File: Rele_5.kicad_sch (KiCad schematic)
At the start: 6 parts, among them J15 Rele_5, J32 Pin GND, K4 SRD-05VDC-SL-C, Q12 PMBT3904,235

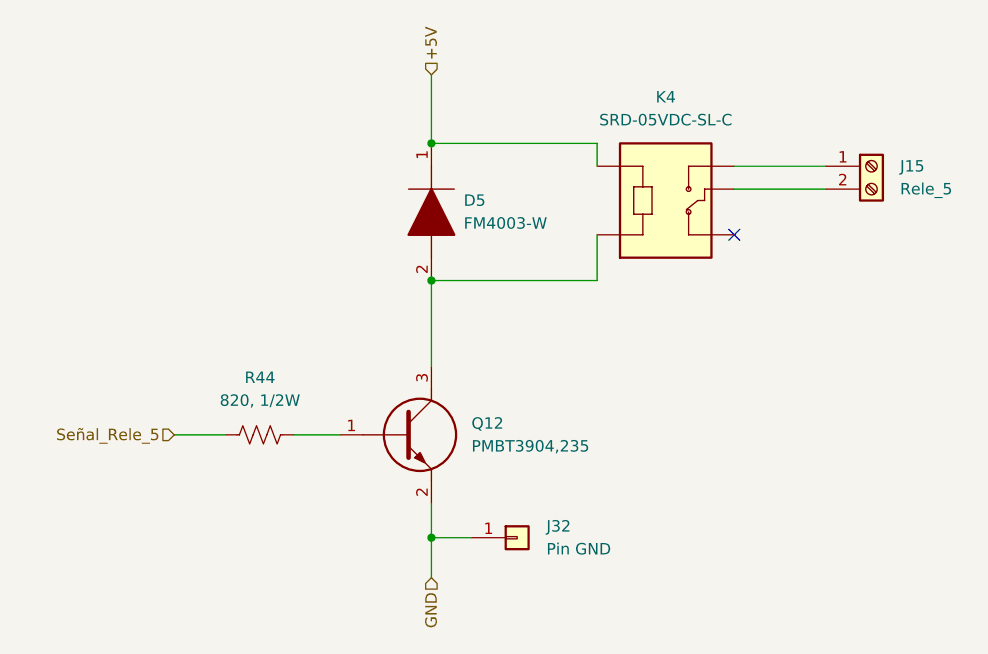
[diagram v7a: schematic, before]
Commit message: Se modificaron algunos componentes, según disponibilidad
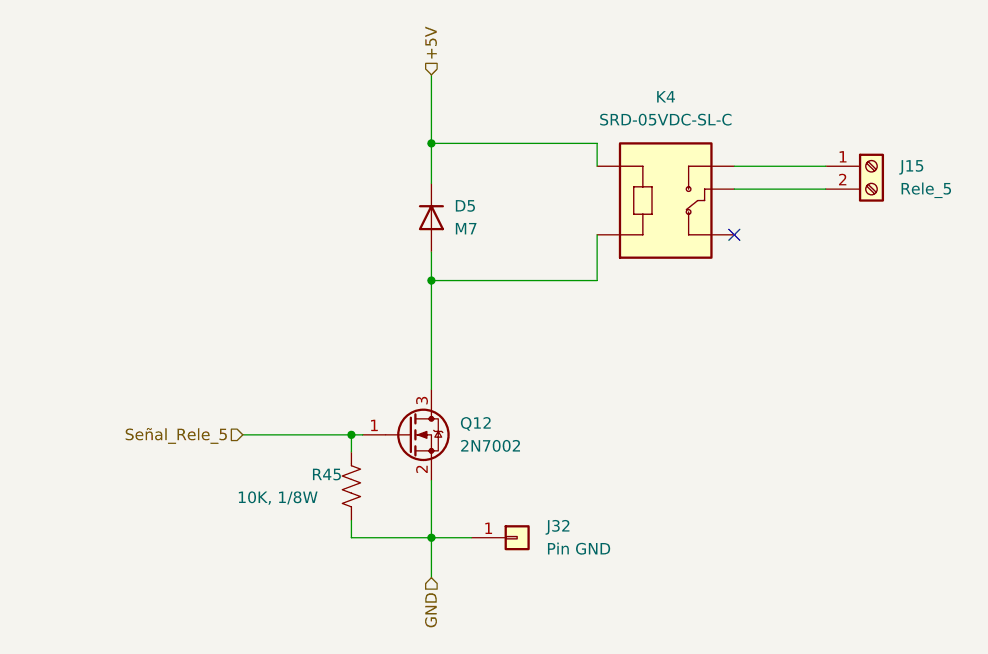
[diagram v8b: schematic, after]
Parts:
- removed D5: FM4003-W, FM4003W:DIOM5025X231N, symbol FM4003-W:FM4003-W
- removed Q12: PMBT3904,235, PMBT3904,235:SOT95P230X110-3N, symbol PMBT3904,235:PMBT3904,235
- removed R44: 820, 1/2W, Resistor_SMD:R_0805_2012Metric, symbol Device:R_US
- added D5: M7, Diode_SMD:D_SMA, symbol Device:D
- added Q12: 2N7002, Package_TO_SOT_SMD:SOT-23, symbol Transistor_FET:2N7002
- added R45: 10K, 1/8W, Resistor_SMD:R_0805_2012Metric, symbol Device:R_US
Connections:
- net +5V: now also D5.1 (K)
- net GND: now also Q12.2 (S), R45.2
- net Señal_Rele_5: now also Q12.1 (G), R45.1
- net at K4.A2: now also D5.2 (A), Q12.3 (D)
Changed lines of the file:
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@@
 (kicad_sch (version 20211123) (generator eeschema)
   (paper "A4")
+  (junction (at 143.51 90.805) (diameter 0) (color 0 0 0 0)
+  )
   (junction (at 143.51 75.565) (diameter 0) (color 0 0 0 0)
   )
-  (junction (at 143.51 90.805) (diameter 0) (color 0 0 0 0)
+  (junction (at 134.62 107.95) (diameter 0) (color 0 0 0 0)
   )
   (junction (at 143.51 119.38) (diameter 0) (color 0 0 0 0)
   )
   (no_connect (at 177.165 85.725))
+  (wire (pts (xy 134.62 107.95) (xy 135.89 107.95))
+    (stroke (width 0) (type default) (color 0 0 0 0))
+  )
   (wire (pts (xy 143.51 119.38) (xy 147.955 119.38))
     (stroke (width 0) (type default) (color 0 0 0 0))
@@
     (stroke (width 0) (type default) (color 0 0 0 0))
   )
-  (wire (pts (xy 114.935 107.95) (xy 120.65 107.95))
+  (wire (pts (xy 134.62 107.95) (xy 134.62 109.855))
     (stroke (width 0) (type default) (color 0 0 0 0))
   )
@@
     (stroke (width 0) (type default) (color 0 0 0 0))
   )
-  (wire (pts (xy 143.51 115.57) (xy 143.51 119.38))
+  (wire (pts (xy 143.51 87.63) (xy 143.51 90.805))
+    (stroke (width 0) (type default) (color 0 0 0 0))
+  )
+  (wire (pts (xy 143.51 113.03) (xy 143.51 119.38))
+    (stroke (width 0) (type default) (color 0 0 0 0))
+  )
+  (wire (pts (xy 134.62 117.475) (xy 134.62 119.38))
     (stroke (width 0) (type default) (color 0 0 0 0))
   )
@@
     (stroke (width 0) (type default) (color 0 0 0 0))
   )
+  (wire (pts (xy 134.62 119.38) (xy 143.51 119.38))
+    (stroke (width 0) (type default) (color 0 0 0 0))
+  )
   (wire (pts (xy 143.51 119.38) (xy 143.51 123.825))
     (stroke (width 0) (type default) (color 0 0 0 0))
   )
-  (wire (pts (xy 128.27 107.95) (xy 133.35 107.95))
+  (wire (pts (xy 122.555 107.95) (xy 134.62 107.95))
+    (stroke (width 0) (type default) (color 0 0 0 0))
+  )
+  (wire (pts (xy 143.51 75.565) (xy 143.51 80.01))
     (stroke (width 0) (type default) (color 0 0 0 0))
   )
@@
     (stroke (width 0) (type default) (color 0 0 0 0))
   )
-  (wire (pts (xy 143.51 90.805) (xy 143.51 100.33))
+  (wire (pts (xy 143.51 90.805) (xy 143.51 102.87))
     (stroke (width 0) (type default) (color 0 0 0 0))
   )
@@
     (effects (font (size 1.27 1.27)) (justify right))
   )
-  (hierarchical_label "Señal_Rele_5" (shape input) (at 114.935 107.95 180)
+  (hierarchical_label "Señal_Rele_5" (shape input) (at 122.555 107.95 180)
     (effects (font (size 1.27 1.27)) (justify right))
   )
@@
     (pin "NO")
   )
-  (symbol (lib_id "PMBT3904,235:PMBT3904,235") (at 133.35 107.95 0) (unit 1)
-    (in_bom yes) (on_board yes) (fields_autoplaced)
-    (property "Reference" "Q12" (id 0) (at 147.955 106.6799 0)
+  (symbol (lib_id "Device:R_US") (at 134.62 113.665 0) (unit 1)
+    (in_bom yes) (on_board yes)
+    (property "Reference" "R45" (id 0) (at 130.175 112.395 0)
       (effects (font (size 1.27 1.27)) (justify left))
     )
-    (property "Value" "PMBT3904,235" (id 1) (at 147.955 109.2199 0)
+    (property "Value" "10K, 1/8W" (id 1) (at 121.92 114.935 0)
       (effects (font (size 1.27 1.27)) (justify left))
     )
-    (property "Footprint" "PMBT3904,235:SOT95P230X110-3N" (id 2) (at 147.32 111.76 0)
-      (effects (font (size 1.27 1.27)) (justify left) hide)
-    )
-    (property "Datasheet" "https://assets.nexperia.com/documents/data-sheet/PMBT3904.pdf" (id 3) (at 147.32 114.3 0)
-      (effects (font (size 1.27 1.27)) (justify left) hide)
-    )
-    (property "Description" "PMBT3904 - NPN switching transistor" (id 4) (at 147.32 116.84 0)
-      (effects (font (size 1.27 1.27)) (justify left) hide)
-    )
-    (property "Height" "1.1" (id 5) (at 147.32 119.38 0)
-      (effects (font (size 1.27 1.27)) (justify left) hide)
-    )
-    (property "Manufacturer_Name" "Nexperia" (id 6) (at 147.32 121.92 0)
-      (effects (font (size 1.27 1.27)) (justify left) hide)
-    )
-    (property "Manufacturer_Part_Number" "PMBT3904,235" (id 7) (at 147.32 124.46 0)
-      (effects (font (size 1.27 1.27)) (justify left) hide)
-    )
-    (property "Mouser Part Number" "771-PMBT3904235" (id 8) (at 147.32 127 0)
-      (effects (font (size 1.27 1.27)) (justify left) hide)
-    )
-    (property "Mouser Price/Stock" "https://www.mouser.co.uk/ProductDetail/Nexperia/PMBT3904235?qs=LOCUfHb8d9uziIfl4fmvZg%3D%3D" (id 9) (at 147.32 129.54 0)
-      (effects (font (size 1.27 1.27)) (justify left) hide)
-    )
-    (property "Arrow Part Number" "PMBT3904,235" (id 10) (at 147.32 132.08 0)
-      (effects (font (size 1.27 1.27)) (justify left) hide)
-    )
-    (property "Arrow Price/Stock" "https://www.arrow.com/en/products/pmbt3904235/nexperia?region=nac" (id 11) (at 147.32 134.62 0)
-      (effects (font (size 1.27 1.27)) (justify left) hide)
-    )
-    (property "Mouser Testing Part Number" "" (id 12) (at 147.32 137.16 0)
-      (effects (font (size 1.27 1.27)) (justify left) hide)
-    )
-    (property "Mouser Testing Price/Stock" "" (id 13) (at 147.32 139.7 0)
-      (effects (font (size 1.27 1.27)) (justify left) hide)
-    )
-    (pin "1")
-    (pin "2")
-    (pin "3")
-  )
-  (symbol (lib_id "Device:R_US") (at 124.46 107.95 90) (unit 1)
-    (in_bom yes) (on_board yes) (fields_autoplaced)
-    (property "Reference" "R44" (id 0) (at 124.46 101.6 90))
-    (property "Value" "820, 1/2W" (id 1) (at 124.46 104.14 90))
-    (property "Footprint" "Resistor_SMD:R_0805_2012Metric" (id 2) (at 124.714 106.934 90)
+    (property "Footprint" "Resistor_SMD:R_0805_2012Metric" (id 2) (at 135.636 113.919 90)
       (effects (font (size 1.27 1.27)) hide)
     )
-    (property "Datasheet" "~" (id 3) (at 124.46 107.95 0)
+    (property "Datasheet" "~" (id 3) (at 134.62 113.665 0)
       (effects (font (size 1.27 1.27)) hide)
     )
@@
     (pin "2")
   )
+  (symbol (lib_id "Transistor_FET:2N7002") (at 140.97 107.95 0) (unit 1)
+    (in_bom yes) (on_board yes) (fields_autoplaced)
+    (property "Reference" "Q12" (id 0) (at 146.685 106.6799 0)
+      (effects (font (size 1.27 1.27)) (justify left))
+    )
+    (property "Value" "2N7002" (id 1) (at 146.685 109.2199 0)
+      (effects (font (size 1.27 1.27)) (justify left))
+    )
+    (property "Footprint" "Package_TO_SOT_SMD:SOT-23" (id 2) (at 146.05 109.855 0)
+      (effects (font (size 1.27 1.27) italic) (justify left) hide)
+    )
+    (property "Datasheet" "https://www.onsemi.com/pub/Collateral/NDS7002A-D.PDF" (id 3) (at 140.97 107.95 0)
+      (effects (font (size 1.27 1.27)) (justify left) hide)
+    )
+    (pin "1")
+    (pin "2")
+    (pin "3")
+  )
   (symbol (lib_id "Connector_Generic:Conn_01x01") (at 153.035 119.38 0) (unit 1)
     (in_bom yes) (on_board yes) (fields_autoplaced)
@@
     (pin "1")
   )
-  (symbol (lib_id "FM4003-W:FM4003-W") (at 143.51 75.565 270) (unit 1)
+  (symbol (lib_id "Device:D") (at 143.51 83.82 270) (unit 1)
     (in_bom yes) (on_board yes) (fields_autoplaced)
-    (property "Reference" "D5" (id 0) (at 147.0914 81.9149 90)
+    (property "Reference" "D5" (id 0) (at 146.05 82.5499 90)
       (effects (font (size 1.27 1.27)) (justify left))
     )
-    (property "Value" "FM4003-W" (id 1) (at 147.0914 84.4549 90)
+    (property "Value" "M7" (id 1) (at 146.05 85.0899 90)
       (effects (font (size 1.27 1.27)) (justify left))
     )
-    (property "Footprint" "FM4003W:DIOM5025X231N" (id 2) (at 143.51 86.995 0)
-      (effects (font (size 1.27 1.27)) (justify left) hide)
+    (property "Footprint" "Diode_SMD:D_SMA" (id 2) (at 143.51 83.82 0)
+      (effects (font (size 1.27 1.27)) hide)
     )
-    (property "Datasheet" "https://componentsearchengine.com/Datasheets/1/FM4003-W.pdf" (id 3) (at 140.97 86.995 0)
-      (effects (font (size 1.27 1.27)) (justify left) hide)
-    )
-    (property "Description" "Rectifiers 1A 200V GP" (id 4) (at 138.43 86.995 0)
-      (effects (font (size 1.27 1.27)) (justify left) hide)
-    )
-    (property "Height" "2.31" (id 5) (at 135.89 86.995 0)
-      (effects (font (size 1.27 1.27)) (justify left) hide)
-    )
-    (property "Manufacturer_Name" "Rectron" (id 6) (at 133.35 86.995 0)
-      (effects (font (size 1.27 1.27)) (justify left) hide)
-    )
-    (property "Manufacturer_Part_Number" "FM4003-W" (id 7) (at 130.81 86.995 0)
-      (effects (font (size 1.27 1.27)) (justify left) hide)
-    )
-    (property "Mouser Part Number" "583-FM4003-W" (id 8) (at 128.27 86.995 0)
-      (effects (font (size 1.27 1.27)) (justify left) hide)
-    )
-    (property "Mouser Price/Stock" "https://www.mouser.co.uk/ProductDetail/Rectron/FM4003-W/?qs=5h8Q3Z7TNRlJu6QU92Ho0w%3D%3D" (id 9) (at 125.73 86.995 0)
-      (effects (font (size 1.27 1.27)) (justify left) hide)
-    )
-    (property "Arrow Part Number" "FM4003-W" (id 10) (at 123.19 86.995 0)
-      (effects (font (size 1.27 1.27)) (justify left) hide)
-    )
-    (property "Arrow Price/Stock" "https://www.arrow.com/en/products/fm4003-w/rectron" (id 11) (at 120.65 86.995 0)
-      (effects (font (size 1.27 1.27)) (justify left) hide)
-    )
-    (property "Mouser Testing Part Number" "" (id 12) (at 118.11 86.995 0)
-      (effects (font (size 1.27 1.27)) (justify left) hide)
-    )
-    (property "Mouser Testing Price/Stock" "" (id 13) (at 115.57 86.995 0)
-      (effects (font (size 1.27 1.27)) (justify left) hide)
+    (property "Datasheet" "~" (id 3) (at 143.51 83.82 0)
+      (effects (font (size 1.27 1.27)) hide)
     )
     (pin "1")
